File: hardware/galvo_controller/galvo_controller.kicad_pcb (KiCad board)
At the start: 4 copper layers, 75 x 95 mm, 134 parts, among them J1 USB_OTG, J2 Conn_01x03, J3 Conn_01x03, J4 Micro_SD_Card_Det, J5 Red, J6 White, J7 Conn_01x03, J8 Conn_01x03, Q1 MMBT2222, Q2 MMBT2222, SW1 JS1400BFQ, U1 SN74LV1T34, U10 LME49724, U2 UG-2832HSWEG02, U3 CP2104, U4 ESP-WROOM-32D, U5 TPS54295PWP, U6 PCM3060, U7 NCP1117LP, U8 OPA2134, U9 LME49724

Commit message: Working on layout
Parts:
- moved C48 4.11 mm to (196.6, 72.5), turned to 0 degrees
- moved C43 3.51 mm to (196.9, 74.5), turned to 0 degrees
- moved C33 2.96 mm to (192.6, 101.8), turned to 180 degrees
- moved C36 2.76 mm to (192.6, 91.8)
- moved R34 2.42 mm to (192.6, 90.1)
- moved C37 2.36 mm to (192.6, 122.8)
- moved R35 2.30 mm to (192.6, 124.5)
- moved C34 2.25 mm to (192.6, 121.2), turned to 180 degrees
- moved C35 2.25 mm to (192.6, 103.4)
- moved C44 2.18 mm to (196.4, 103.6)
- moved R33 2.15 mm to (192.6, 105.0)
- moved C49 2.14 mm to (196.4, 101.8)
- moved C52 2.14 mm to (196.4, 90.0)
- moved C55 2.11 mm to (196.4, 91.8)
- moved C53 1.92 mm to (196.4, 109.3), turned to 0 degrees
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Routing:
- net /VCOM: track 7.28 -> 39.4 mm, vias 0 -> 2
- net GNDA: track 80.1 -> 100.5 mm, vias 62 -> 80
- net VCC: track 25.3 -> 42.1 mm, vias 6 -> 9
- net Net-(C38-Pad1): track 0.00 -> 15.0 mm
- net VEE: track 10.6 -> 25.2 mm, vias 1 -> 2
- net Net-(C36-Pad1): track 0.00 -> 14.5 mm
- net Net-(C37-Pad1): track 0.00 -> 13.4 mm
- net Net-(C35-Pad1): track 0.00 -> 13.4 mm
- net Net-(C37-Pad2): track 0.00 -> 9.62 mm
- net Net-(C35-Pad2): track 0.00 -> 9.58 mm
- net Net-(C36-Pad2): track 0.00 -> 8.08 mm
- net Net-(C38-Pad2): track 0.00 -> 8.02 mm
- net /X_P: track 0.00 -> 6.65 mm
- net /X_N: track 0.00 -> 6.45 mm
- net /Y_P: track 0.00 -> 6.07 mm
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
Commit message: Working on layout
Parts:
- moved C33 1.40 mm to (192.6, 103.2)
- moved C36 1.40 mm to (192.6, 93.2)
- moved C44 1.40 mm to (196.4, 105.0)
- moved C49 1.40 mm to (196.4, 103.2)
- moved C52 1.40 mm to (196.4, 91.4)
- moved C55 1.40 mm to (196.4, 93.2)
- moved R27 1.40 mm to (189.5, 99.2)
- moved R28 1.40 mm to (189.5, 97.2)
- moved R33 1.40 mm to (192.6, 106.4)
- moved R34 1.40 mm to (192.6, 91.5)
- moved R39 1.40 mm to (199.3, 99.2)
- moved R40 1.40 mm to (199.3, 97.2)
- moved U9 1.40 mm to (194.5, 98.2)
- moved C35 1.40 mm to (192.6, 104.8)
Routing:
- net /VOUTL_P: track 16.1 -> 17.9 mm
- net /VOUTL_N: track 16.1 -> 17.9 mm
- net /X_P: track 6.65 -> 6.07 mm

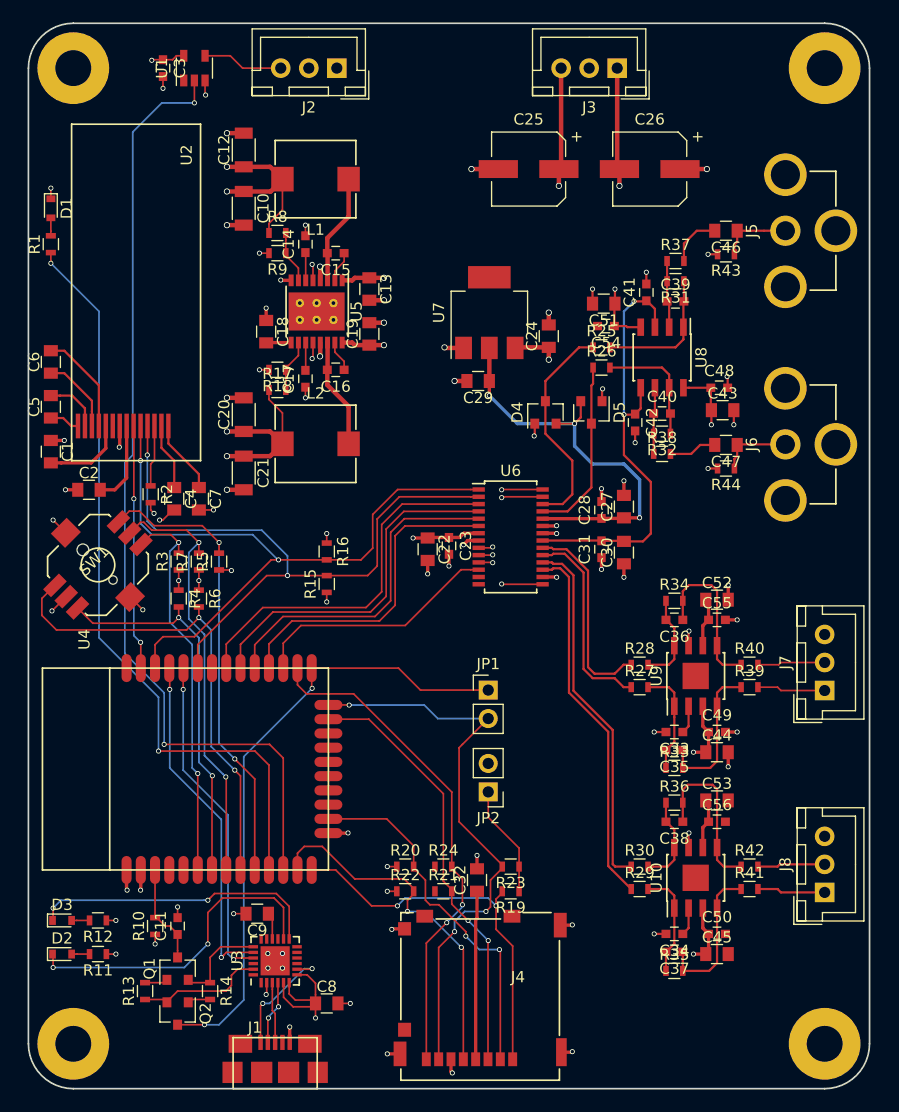
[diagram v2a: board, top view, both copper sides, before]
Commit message: Finished routing board
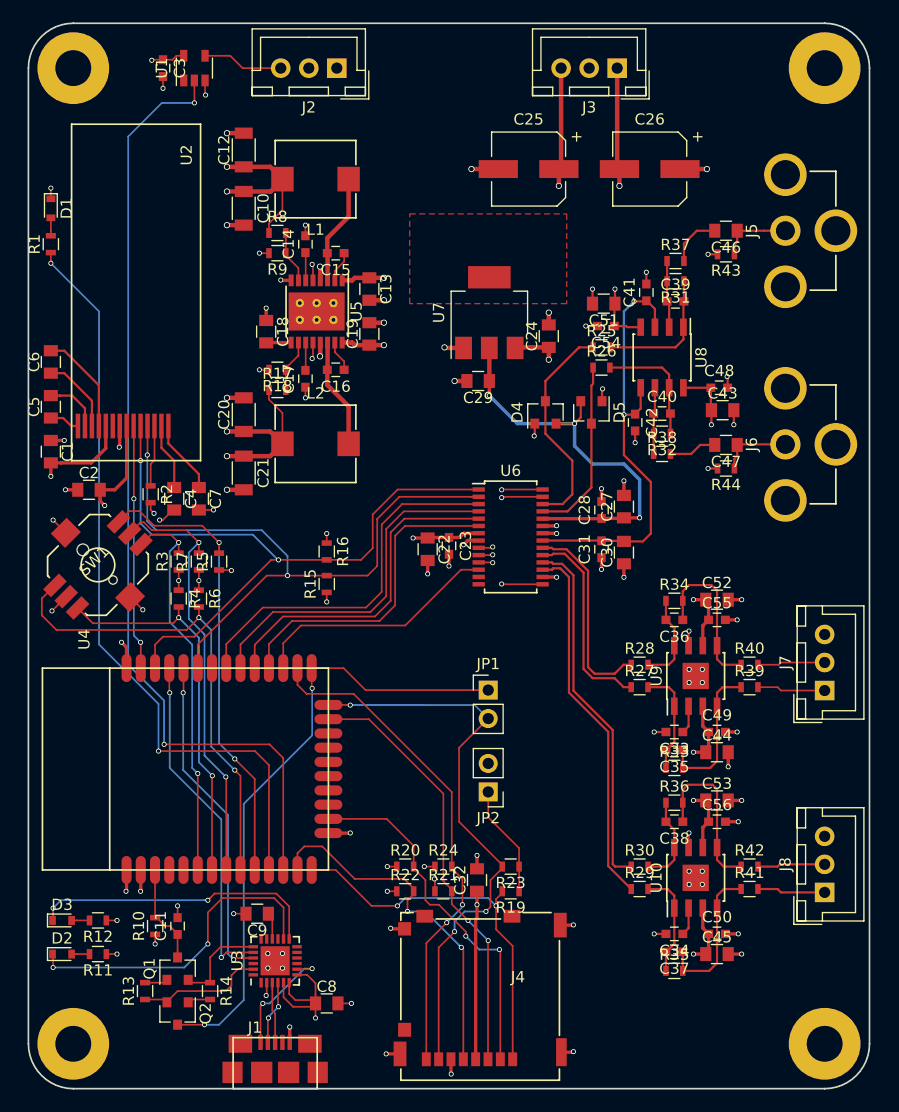
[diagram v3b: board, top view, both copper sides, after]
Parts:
- U7: footprint TO_SOT_Packages_SMD:SOT-223 -> TO_SOT_Packages_SMD:SOT-223-3_TabPin2
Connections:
- J1 pad 4: (no net) -> Net-(J1-Pad4)
- J4 pad 10: (no net) -> Net-(J4-Pad10)
- U2 pad 6: (no net) -> Net-(U2-Pad6)
- U3 pad 1: (no net) -> Net-(U3-Pad1)
- U3 pad 10: (no net) -> Net-(U3-Pad10)
- U3 pad 11: (no net) -> Net-(U3-Pad11)
- U3 pad 12: (no net) -> Net-(U3-Pad12)
- U3 pad 15: (no net) -> Net-(U3-Pad15)
- U3 pad 17: (no net) -> Net-(U3-Pad17)
- U3 pad 18: (no net) -> Net-(U3-Pad18)
- U3 pad 22: (no net) -> Net-(U3-Pad22)
- U3 pad 24: (no net) -> Net-(U3-Pad24)
- U3 pad 9: (no net) -> Net-(U3-Pad9)
- U4 pad 17: (no net) -> Net-(U4-Pad17)
- U4 pad 18: (no net) -> Net-(U4-Pad18)
- U4 pad 19: (no net) -> Net-(U4-Pad19)
- U4 pad 20: (no net) -> Net-(U4-Pad20)
- U4 pad 21: (no net) -> Net-(U4-Pad21)
- U4 pad 22: (no net) -> Net-(U4-Pad22)
- U4 pad 32: (no net) -> Net-(U4-Pad32)
- U4 pad 4: (no net) -> Net-(U4-Pad4)
- U4 pad 5: (no net) -> Net-(U4-Pad5)
- U6 pad 13: (no net) -> Net-(U6-Pad13)
- U6 pad 14: (no net) -> Net-(U6-Pad14)
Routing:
- net GNDA: track 100.5 -> 109.7 mm, vias 80 -> 86
- net /SD_DAT0: track 51.3 -> 57.9 mm
- net +3V3: track 81.6 -> 86.7 mm, vias 16 -> 21
- net VEE: track 25.2 -> 27.4 mm, vias 2 -> 12
- added copper zone on F.Cu, net +5VA

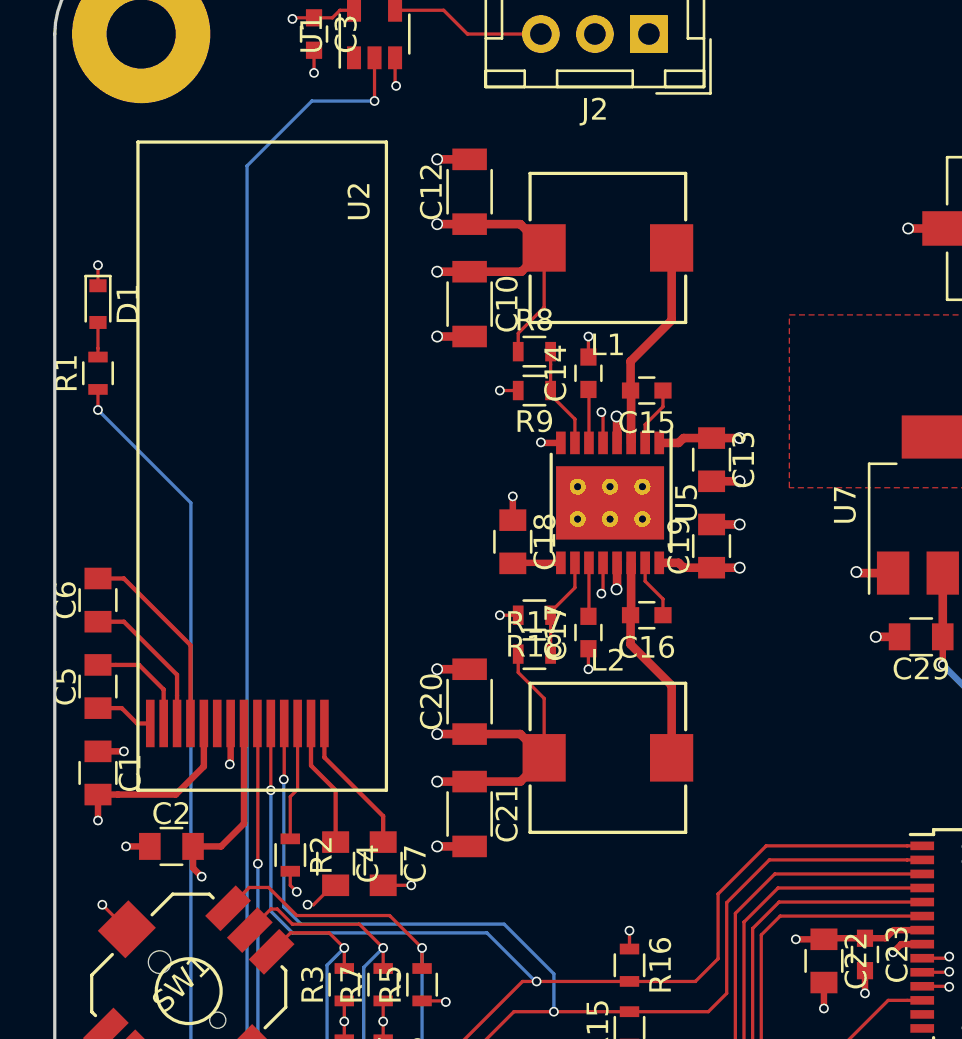
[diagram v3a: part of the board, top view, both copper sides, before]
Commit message: Adjusted oled footprint
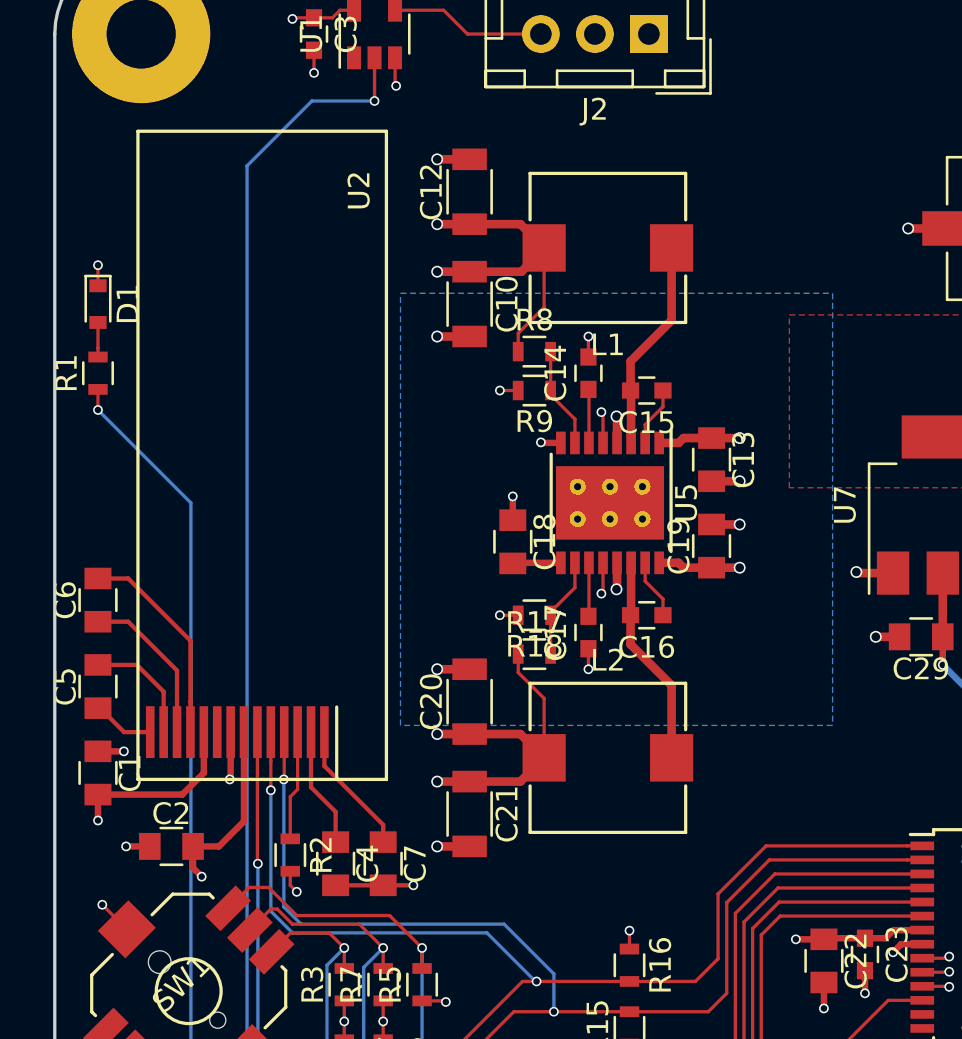
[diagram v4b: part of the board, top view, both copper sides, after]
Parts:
- moved U2 0.50 mm to (144.6, 63.5)
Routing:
- net GNDA: track 109.7 -> 110.6 mm, vias 86 -> 85
- net +3V3: track 86.7 -> 86.0 mm
- net Net-(C6-Pad1): track 6.93 -> 7.45 mm
- net Net-(C6-Pad2): track 9.19 -> 9.70 mm
- added copper zone on B.Cu, net GNDA
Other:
- rule pad_to_mask_clearance: 0.2 -> 0

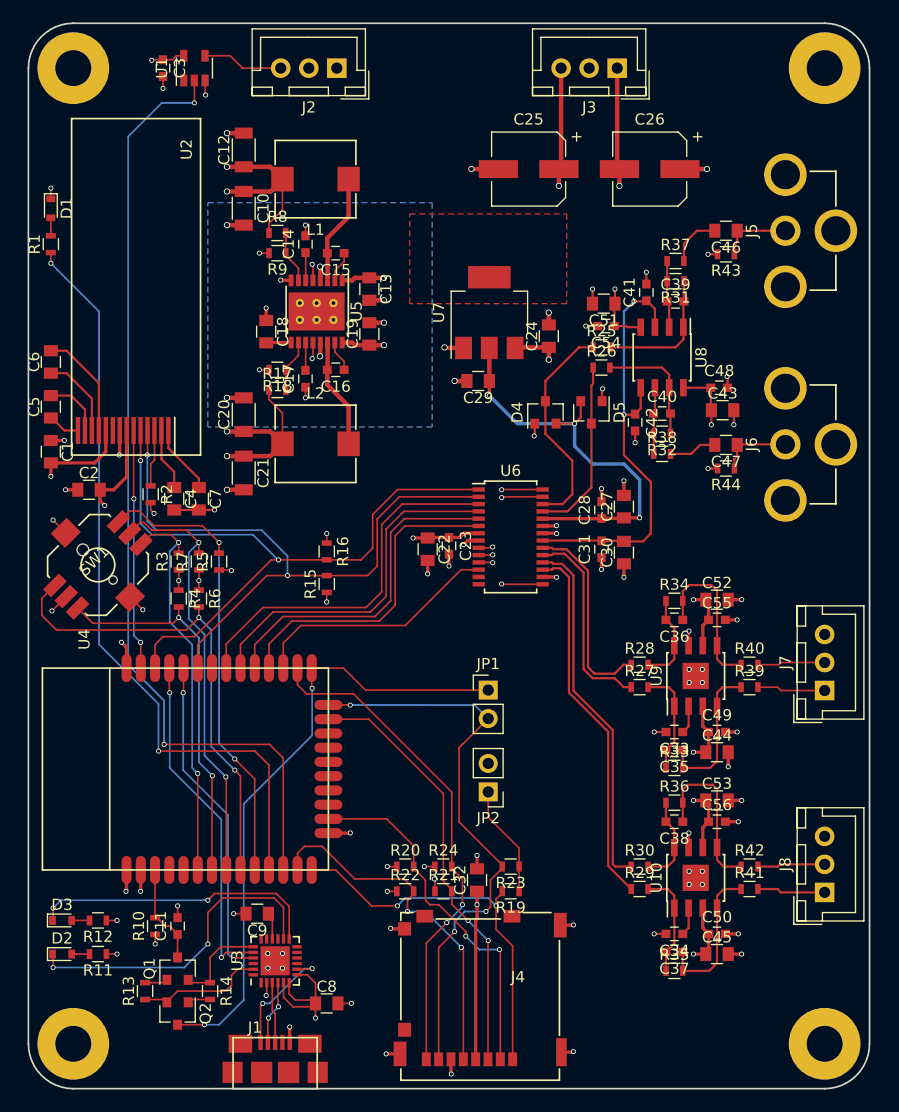
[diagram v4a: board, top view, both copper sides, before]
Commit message: Adding silkscreen text
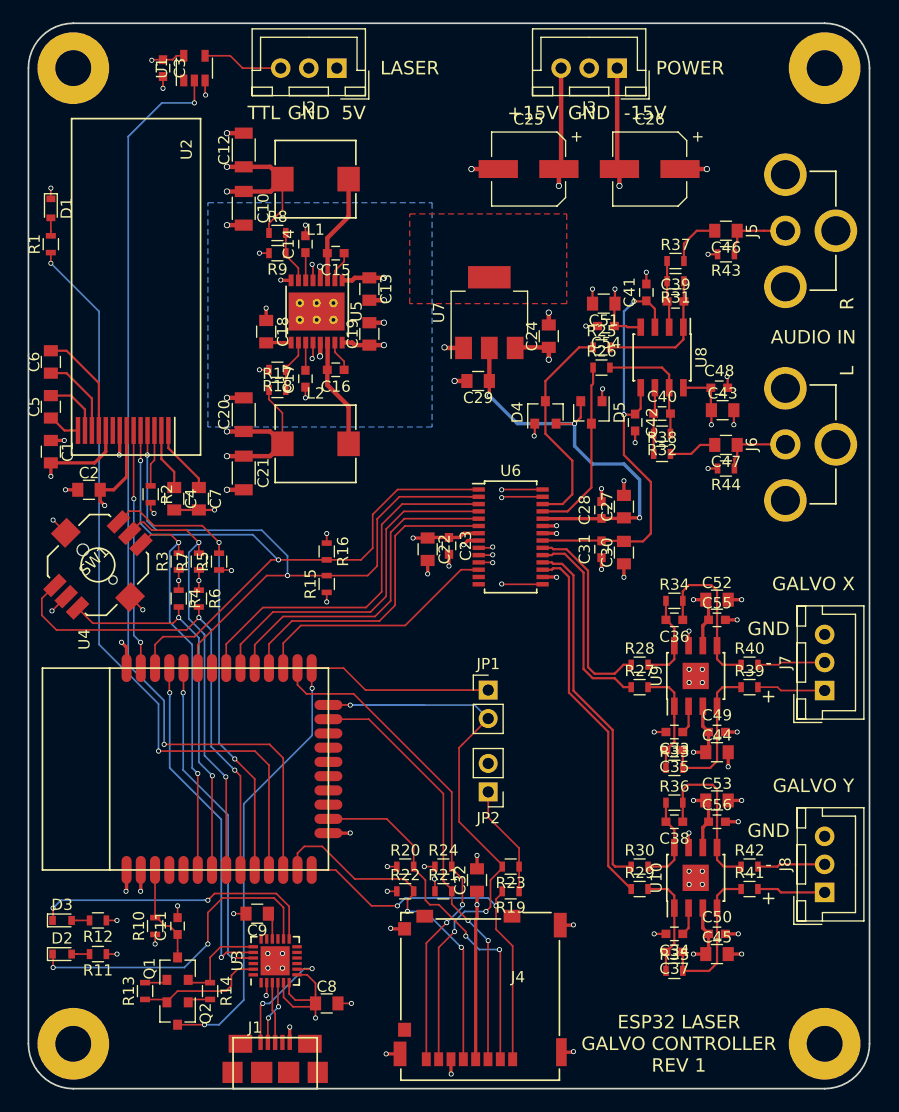
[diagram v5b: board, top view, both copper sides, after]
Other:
- board text added: "+"
- board text added: "+15V"
- board text added: "-"
- board text added: "-15V"
- board text added: "5V"
- board text added: "AUDIO IN"
- board text added: "ESP32 LASER GALVO CONTROLLER REV 1"
- board text added: "GALVO X"
- board text added: "GALVO Y"
- board text added: "GND"
- board text added: "L"
- board text added: "LASER"
- board text added: "POWER"
- board text added: "R"
- board text added: "TTL"
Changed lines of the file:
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@@
     (area 134.924999 39.924999 210.075001 135.075001)
     (thickness 1.6)
-    (drawings 8)
+    (drawings 28)
     (tracks 1031)
     (zones 0)
@@
     (0 F.Cu signal)
     (1 In1.Cu signal hide)
-    (2 In2.Cu signal)
+    (2 In2.Cu signal hide)
     (31 B.Cu signal)
     (35 F.Paste user)
@@
   )
   (setup
-    (last_trace_width 0.2)
+    (last_trace_width 0.16)
     (user_trace_width 0.16)
     (user_trace_width 0.2)
@@
     )
   )
+  (gr_text L (at 208 71 90) (layer F.SilkS)
+    (effects (font (size 1.2 1.2) (thickness 0.2)))
+  )
+  (gr_text R (at 208 65 90) (layer F.SilkS)
+    (effects (font (size 1.2 1.2) (thickness 0.2)))
+  )
+  (gr_text "AUDIO IN" (at 205 68) (layer F.SilkS)
+    (effects (font (size 1.2 1.2) (thickness 0.2)))
+  )
+  (gr_text + (at 201 118) (layer F.SilkS)
+    (effects (font (size 1.2 1.2) (thickness 0.2)))
+  )
+  (gr_text - (at 201 115) (layer F.SilkS)
+    (effects (font (size 1.2 1.2) (thickness 0.2)))
+  )
+  (gr_text + (at 201 100) (layer F.SilkS)
+    (effects (font (size 1.2 1.2) (thickness 0.2)))
+  )
+  (gr_text - (at 201 97) (layer F.SilkS)
+    (effects (font (size 1.2 1.2) (thickness 0.2)))
+  )
+  (gr_text GND (at 201 112) (layer F.SilkS)
+    (effects (font (size 1.2 1.2) (thickness 0.2)))
+  )
+  (gr_text GND (at 201 94) (layer F.SilkS)
+    (effects (font (size 1.2 1.2) (thickness 0.2)))
+  )
+  (gr_text "GALVO Y" (at 205 108) (layer F.SilkS)
+    (effects (font (size 1.2 1.2) (thickness 0.2)))
+  )
+  (gr_text "GALVO X" (at 205 90) (layer F.SilkS)
+    (effects (font (size 1.2 1.2) (thickness 0.2)))
+  )
+  (gr_text POWER (at 194 44) (layer F.SilkS)
+    (effects (font (size 1.2 1.2) (thickness 0.2)))
+  )
+  (gr_text LASER (at 169 44) (layer F.SilkS)
+    (effects (font (size 1.2 1.2) (thickness 0.2)))
+  )
+  (gr_text -15V (at 190 48) (layer F.SilkS)
+    (effects (font (size 1.2 1.2) (thickness 0.2)))
+  )
+  (gr_text GND (at 185 48) (layer F.SilkS)
+    (effects (font (size 1.2 1.2) (thickness 0.2)))
+  )
+  (gr_text +15V (at 180 48) (layer F.SilkS)
+    (effects (font (size 1.2 1.2) (thickness 0.2)))
+  )
+  (gr_text 5V (at 164 48) (layer F.SilkS)
+    (effects (font (size 1.2 1.2) (thickness 0.2)))
+  )
+  (gr_text GND (at 160 48) (layer F.SilkS)
+    (effects (font (size 1.2 1.2) (thickness 0.2)))
+  )
+  (gr_text TTL (at 156 48) (layer F.SilkS)
+    (effects (font (size 1.2 1.2) (thickness 0.2)))
+  )
+  (gr_text "ESP32 LASER\nGALVO CONTROLLER\nREV 1" (at 193 131) (layer F.SilkS)
+    (effects (font (size 1.2 1.2) (thickness 0.25)))
+  )
   (gr_arc (start 139 131) (end 139 135) (angle 90) (layer Edge.Cuts) (width 0.15))

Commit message: Cleaned up reference designators, finalizing layout
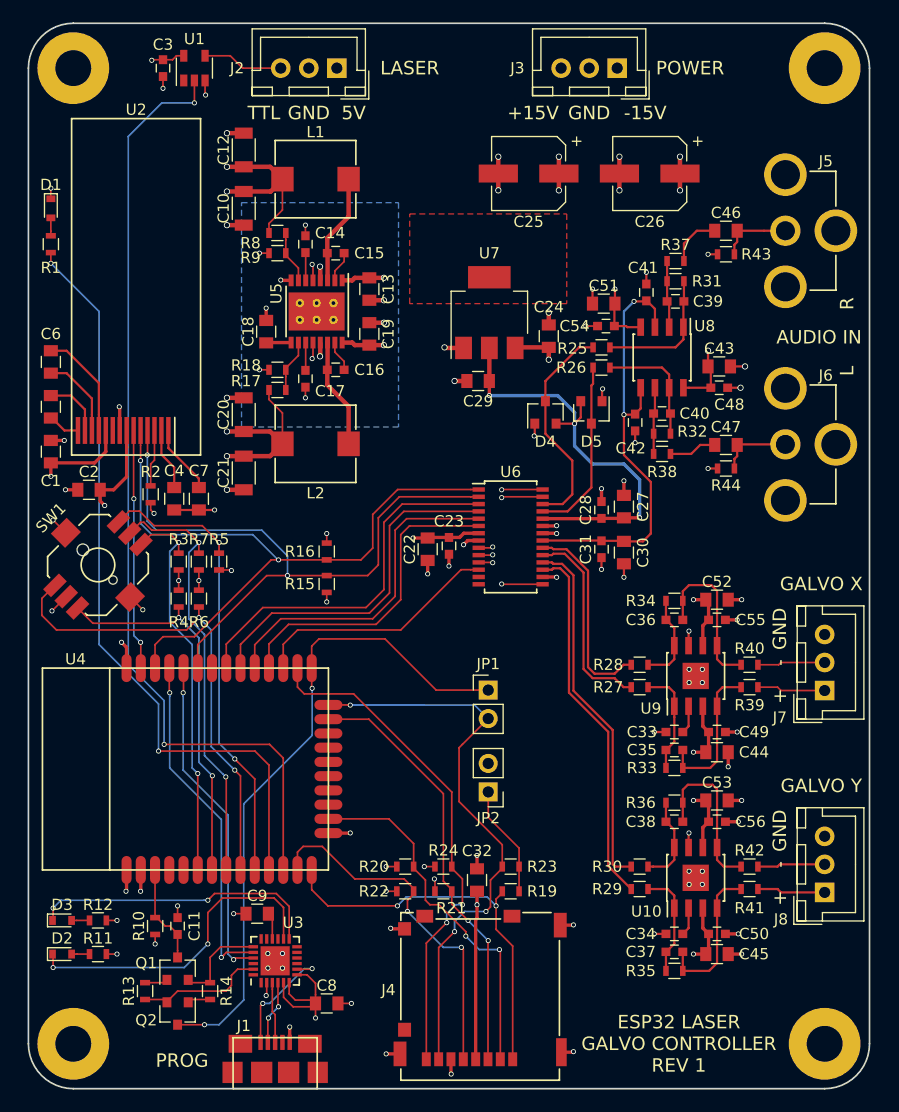
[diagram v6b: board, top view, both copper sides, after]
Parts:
- moved C43 3.91 mm to (196.6, 70.6)
- moved C25 0.40 mm to (179.6, 53.4)
- moved C26 0.40 mm to (190.4, 53.4)
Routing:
- net VEE: track 27.4 -> 19.8 mm, vias 12 -> 13
- net VCC: track 42.1 -> 34.6 mm, vias 9 -> 10
- net /GPIO0: track 55.5 -> 58.8 mm
- net GNDA: track 110.6 -> 111.9 mm, vias 85 -> 87
- net /SD_DAT2: track 34.3 -> 35.4 mm
- net +5VA: track 37.9 -> 38.5 mm
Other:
- board text added: "PROG"
